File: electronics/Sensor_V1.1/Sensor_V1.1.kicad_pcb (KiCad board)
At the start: 2 copper layers, 45.9 x 25.6 mm, 34 parts, among them J1 nuclone_small_left, J2 nuclone_small_right, J5 DevBoardUartInput, Q1 DMG1012, Q2 DMG1012, Q3 DMG1012, U1 PPG_sensor, U2 reference_sot23-3, U3 MCP6541

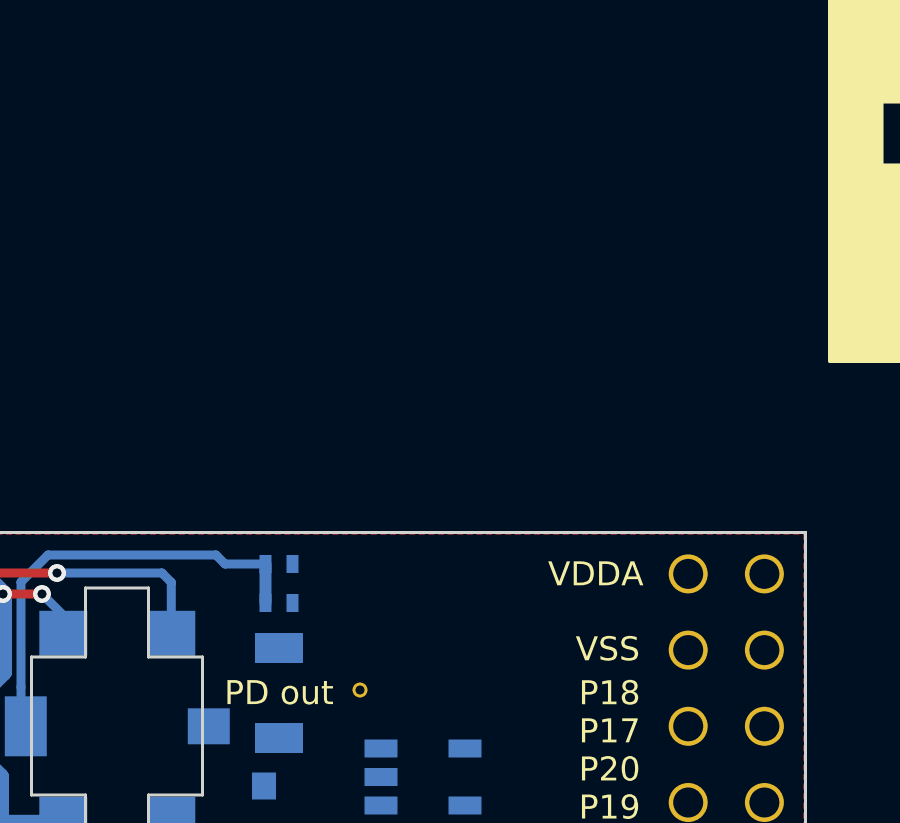
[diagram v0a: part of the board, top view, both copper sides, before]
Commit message: starting to move analog stuff to VSSA and then to star grounds/vcc's. imported net ties
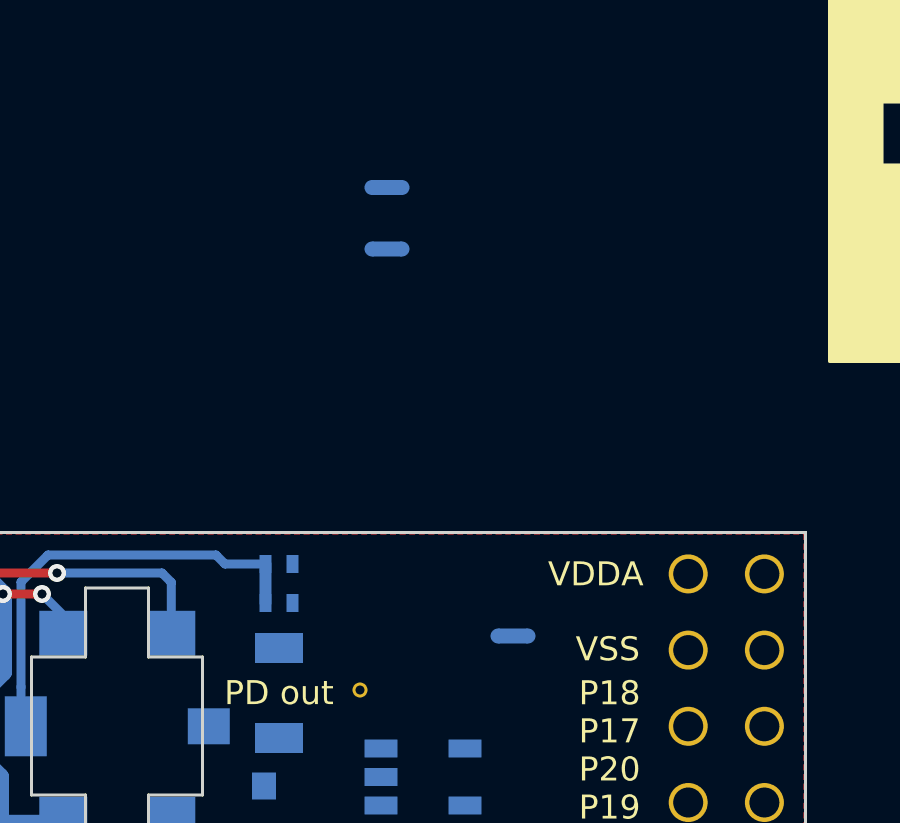
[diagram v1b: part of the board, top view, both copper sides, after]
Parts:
- added NT1: VSS_PD, NetTie:NetTie-2_SMD_Pad0.5mm, B.Cu at (94.1, 64.1)
- added NT2: VSS_CMP, NetTie:NetTie-2_SMD_Pad0.5mm, B.Cu at (94.1, 62.0)
- added NT3: VDD_CMP, NetTie:NetTie-2_SMD_Pad0.5mm, B.Cu at (98.3, 77.0)
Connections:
- C10 pad 2: /VSSA -> /VSS_CMP
- U3 pad 2: /VSSA -> /VSS_CMP
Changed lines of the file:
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@@
     (tracks 79)
     (zones 0)
-    (modules 34)
-    (nets 50)
+    (modules 37)
+    (nets 52)
   )
   (page A4)
@@
   (net 48 /PIO0_20)
   (net 49 /PIO0_19)
+  (net 50 /VSS_CMP)
+  (net 51 /VDD_CMP)
   (net_class Default "This is the default net class."
     (clearance 0.127)
@@
     (add_net /VDD)
     (add_net /VDDA)
+    (add_net /VDD_CMP)
     (add_net /VREF)
     (add_net /VSS)
     (add_net /VSSA)
+    (add_net /VSS_CMP)
     (add_net /VSS_PD)
     (add_net "Net-(J1-Pad11)")
@@
     (add_net "Net-(R17-Pad2)")
   )
+  (module NetTie:NetTie-2_SMD_Pad0.5mm (layer B.Cu)
+    (at 98.3 77)
+    (descr "Net tie, 2 pin, 0.5mm square SMD pads")
+    (tags "net tie")
+    (attr virtual)
+    (fp_text reference NT3 (at 0 1.2) (layer B.SilkS)
+      (effects (font (size 1 1) (thickness 0.15)) (justify mirror))
+    )
+    (fp_text value VDD_CMP (at 0 -1.2) (layer B.Fab)
+      (effects (font (size 1 1) (thickness 0.15)) (justify mirror))
+    )
+    (fp_poly (pts (xy -0.5 0.25) (xy 0.5 0.25) (xy 0.5 -0.25) (xy -0.5 -0.25)) (layer B.Cu) (width 0))
+    (fp_line (start 1 0.5) (end -1 0.5) (layer B.CrtYd) (width 0.05))
+    (fp_line (start 1 -0.5) (end 1 0.5) (layer B.CrtYd) (width 0.05))
+    (fp_line (start -1 -0.5) (end 1 -0.5) (layer B.CrtYd) (width 0.05))
+    (fp_line (start -1 0.5) (end -1 -0.5) (layer B.CrtYd) (width 0.05))
+    (pad 2 smd circle (at 0.5 0) (size 0.5 0.5) (layers B.Cu)
+      (net 51 /VDD_CMP))
+    (pad 1 smd circle (at -0.5 0) (size 0.5 0.5) (layers B.Cu)
+      (net 3 /VDD))
+  )
+  (module NetTie:NetTie-2_SMD_Pad0.5mm (layer B.Cu)
+    (at 94.1 62.05)
+    (descr "Net tie, 2 pin, 0.5mm square SMD pads")
+    (tags "net tie")
+    (attr virtual)
+    (fp_text reference NT2 (at 0 1.2) (layer B.SilkS)
+      (effects (font (size 1 1) (thickness 0.15)) (justify mirror))
+    )
+    (fp_text value VSS_CMP (at 0 -1.2) (layer B.Fab)
+      (effects (font (size 1 1) (thickness 0.15)) (justify mirror))
+    )
+    (fp_poly (pts (xy -0.5 0.25) (xy 0.5 0.25) (xy 0.5 -0.25) (xy -0.5 -0.25)) (layer B.Cu) (width 0))
+    (fp_line (start 1 0.5) (end -1 0.5) (layer B.CrtYd) (width 0.05))
+    (fp_line (start 1 -0.5) (end 1 0.5) (layer B.CrtYd) (width 0.05))
+    (fp_line (start -1 -0.5) (end 1 -0.5) (layer B.CrtYd) (width 0.05))
+    (fp_line (start -1 0.5) (end -1 -0.5) (layer B.CrtYd) (width 0.05))
+    (pad 2 smd circle (at 0.5 0) (size 0.5 0.5) (layers B.Cu)
+      (net 50 /VSS_CMP))
+    (pad 1 smd circle (at -0.5 0) (size 0.5 0.5) (layers B.Cu)
+      (net 2 /VSS))
+  )
+  (module NetTie:NetTie-2_SMD_Pad0.5mm (layer B.Cu)
+    (at 94.1 64.1)
+    (descr "Net tie, 2 pin, 0.5mm square SMD pads")
+    (tags "net tie")
+    (attr virtual)
+    (fp_text reference NT1 (at 0 1.2) (layer B.SilkS)
+      (effects (font (size 1 1) (thickness 0.15)) (justify mirror))
+    )
+    (fp_text value VSS_PD (at 0 -1.2) (layer B.Fab)
+      (effects (font (size 1 1) (thickness 0.15)) (justify mirror))
+    )
+    (fp_poly (pts (xy -0.5 0.25) (xy 0.5 0.25) (xy 0.5 -0.25) (xy -0.5 -0.25)) (layer B.Cu) (width 0))
+    (fp_line (start 1 0.5) (end -1 0.5) (layer B.CrtYd) (width 0.05))
+    (fp_line (start 1 -0.5) (end 1 0.5) (layer B.CrtYd) (width 0.05))
+    (fp_line (start -1 -0.5) (end 1 -0.5) (layer B.CrtYd) (width 0.05))
+    (fp_line (start -1 0.5) (end -1 -0.5) (layer B.CrtYd) (width 0.05))
+    (pad 2 smd circle (at 0.5 0) (size 0.5 0.5) (layers B.Cu)
+      (net 43 /VSS_PD))
+    (pad 1 smd circle (at -0.5 0) (size 0.5 0.5) (layers B.Cu)
+      (net 2 /VSS))
+  )
   (module SquantorRcl:R_0402_hand (layer B.Cu)
     (at 97 84.7 90)
@@
     (fp_line (start 0 0.2) (end 0 -0.2) (layer B.SilkS) (width 0.15))
     (pad 2 smd rect (at 0.55 0 180) (size 0.6 0.6) (layers B.Cu B.Paste B.Mask)
-      (net 5 /VSSA))
+      (net 50 /VSS_CMP))
     (pad 1 smd rect (at -0.55 0 180) (size 0.6 0.6) (layers B.Cu B.Paste B.Mask)
       (net 4 /VDDA))
@@
       (net 14 /PD_OUT))
     (pad 2 smd rect (at 0 -1.4 90) (size 0.6 1.1) (layers B.Cu B.Paste B.Mask)
-      (net 5 /VSSA))
+      (net 50 /VSS_CMP))
     (pad 1 smd rect (at -0.95 -1.4 90) (size 0.6 1.1) (layers B.Cu B.Paste B.Mask)
       (net 18 /CMP_OUT))

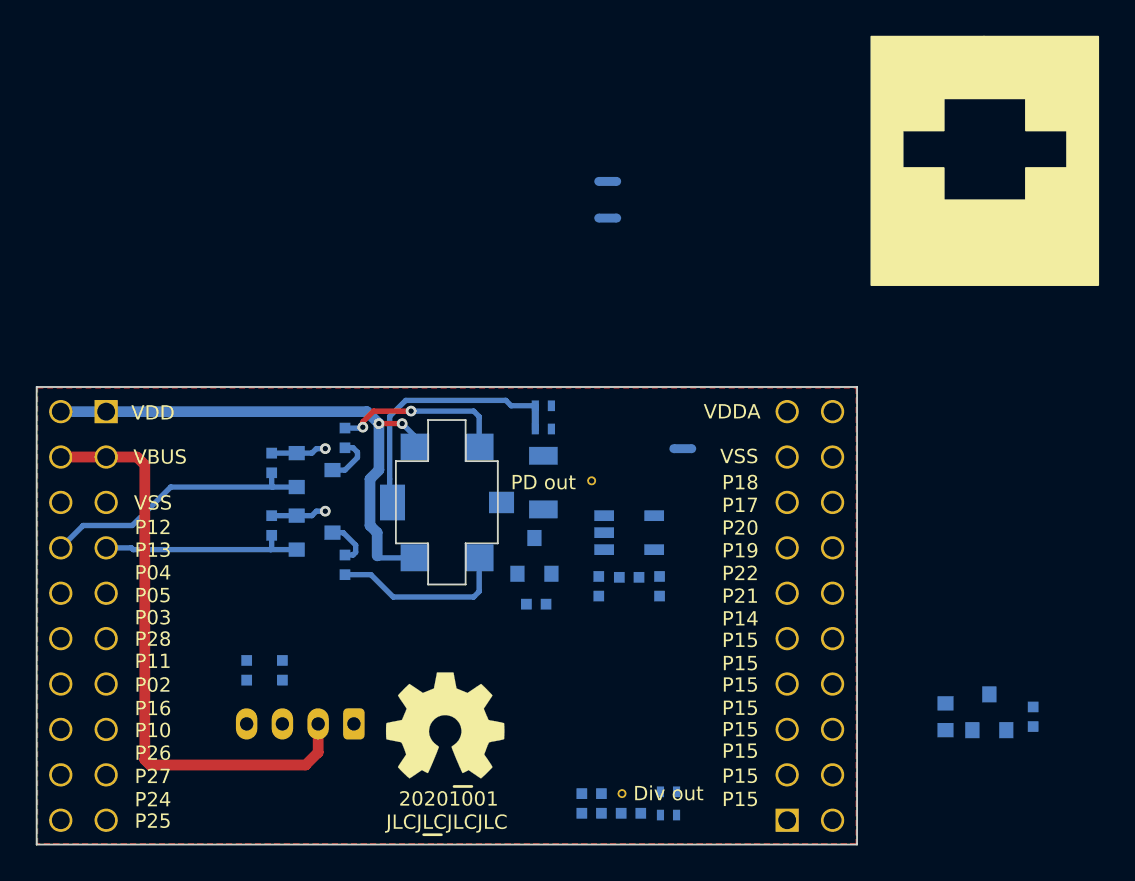
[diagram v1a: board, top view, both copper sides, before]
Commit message: placement of components
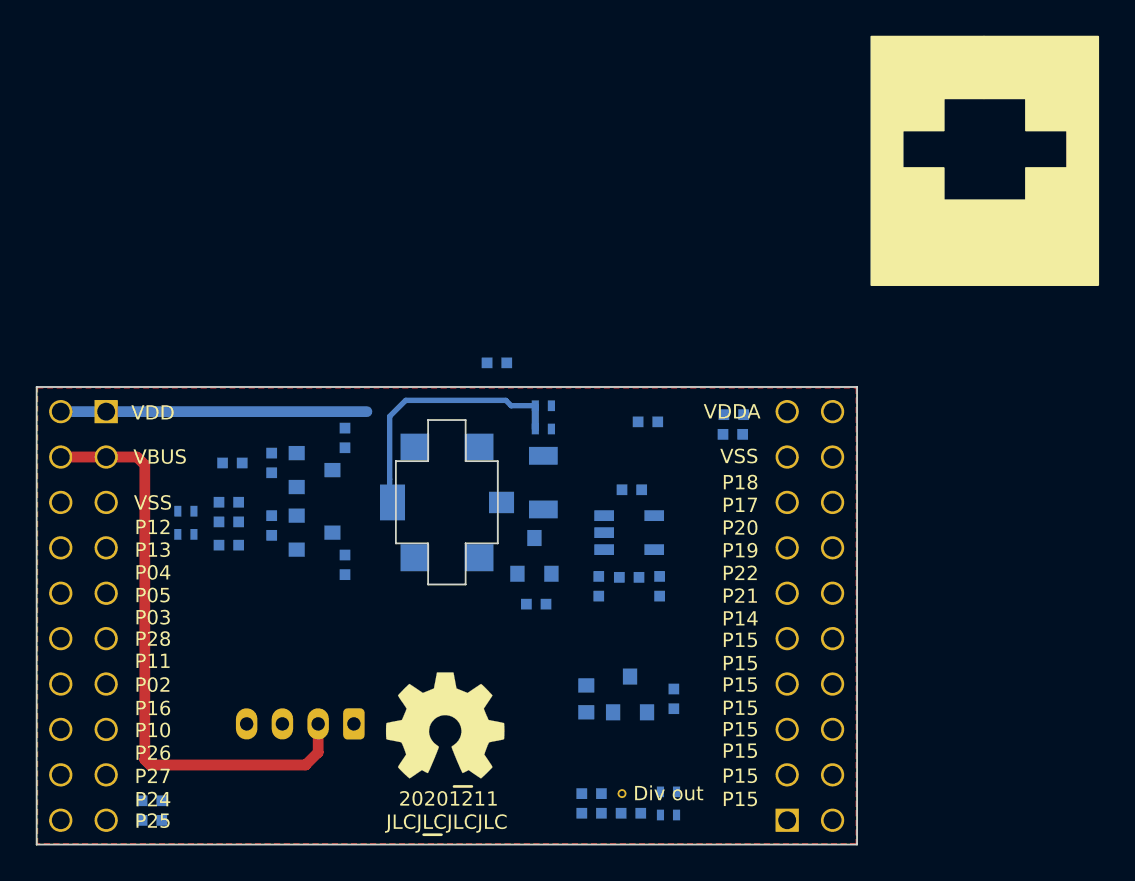
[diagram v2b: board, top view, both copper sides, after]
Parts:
- removed NT1: VSS_PD, NetTie:NetTie-2_SMD_Pad0.5mm
- removed NT2: VSS_CMP, NetTie:NetTie-2_SMD_Pad0.5mm
- removed NT3: VDD_CMP, NetTie:NetTie-2_SMD_Pad0.5mm
- removed TP10: PD out, SquantorTestPoints:TestPoint_hole_H03R05
- added C1: 1u, SquantorRcl:C_0402, B.Cu at (87.9, 72.2)
- added C2: 100n, SquantorRcl:C_0402, B.Cu at (72.9, 81.1)
- added C3: 100n, SquantorRcl:C_0402, B.Cu at (72.9, 82.4)
- added FB1: Ferrite_Bead, SquantorRcl:L_0402, B.Cu at (101.2, 75.1)
- added FB2: Ferrite_Bead, SquantorRcl:L_0402, B.Cu at (101.1, 76.2)
- added FB3: Ferrite_Bead, SquantorRcl:L_0402, B.Cu at (96.3, 75.5)
- added JP2: LED_VDD, SquantorSpecial:solder_jumper_2way_noconn, B.Cu at (70.5, 81.8)
- added JP6: LED_VBUS, SquantorSpecial:solder_jumper_2way_noconn, B.Cu at (70.5, 80.5)
- added R10: 1K, SquantorRcl:R_0402_hand, B.Cu at (73.1, 77.8)
- added R11: 1K, SquantorRcl:R_0402_hand, B.Cu at (72.9, 80.0)
- added R9: 0, SquantorRcl:R_0402_hand, B.Cu at (95.5, 79.3)
- N2: value 20201001 -> 20201211
- R3, R4: value 1K -> 100
- moved C5 20.1 mm to (97.8, 91.0)
- moved U2 20.1 mm to (95.3, 90.8)
- moved C6 20.1 mm to (92.9, 91.0)
- moved R2 11.1 mm to (68.6, 97.8), turned to 0 degrees
- moved R1 9.02 mm to (68.6, 96.7), turned to 0 degrees
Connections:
- net /LED1 renamed /LED1_C
- net /LED2 renamed /LED2_C
- net /PIO0_19 renamed Net-(J2-Pad13)
- net /PIO0_20 renamed Net-(J2-Pad14)
- net /PIO_11 renamed Net-(J1-Pad14)
- net /PIO_3 renamed Net-(J1-Pad12)
- C10 pad 1: /VDDA -> Net-(C10-Pad1)
- C10 pad 2: /VSS_CMP -> /VSS
- C11 pad 1: /VSSA -> /VSS
- C5 pad 1: /VDD -> Net-(C5-Pad1)
- C9 pad 2: /VSS_PD -> /VSS
- J1 pad 3: /VBUS -> Net-(J1-Pad3)
- J1 pad 5: /VSS -> Net-(J1-Pad5)
- J2 pad 15: /PIO0_17 -> /CMP_OUT
- J2 pad 16: /PIO0_18 -> /PD_ADC
- J2 pad 17: /VSS -> Net-(J2-Pad17)
- R12 pad 1: /VSSA -> /VSS
- U1 pad 1: /VDD -> /LED1_A
- U1 pad 3: /VDD -> /LED2_A
- U2 pad 1: /VDD -> Net-(C5-Pad1)
- U3 pad 2: /VSS_CMP -> /VSS
- U3 pad 5: /VDDA -> Net-(C10-Pad1)
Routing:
- net /LED2_EN: track 15.4 -> 0.00 mm
- net /VDD: track 30.9 -> 17.1 mm, vias 2 -> 0
- net /LED1_EN: track 11.5 -> 0.00 mm
- net /LED1_C: track 10.0 -> 0.00 mm
- net /LED2_C: track 9.91 -> 0.00 mm, vias 2 -> 0
- net /VSS: track 6.21 -> 0.00 mm, vias 2 -> 0
- net Net-(Q3-Pad3): track 2.79 -> 0.00 mm
- net Net-(Q2-Pad3): track 2.65 -> 0.00 mm

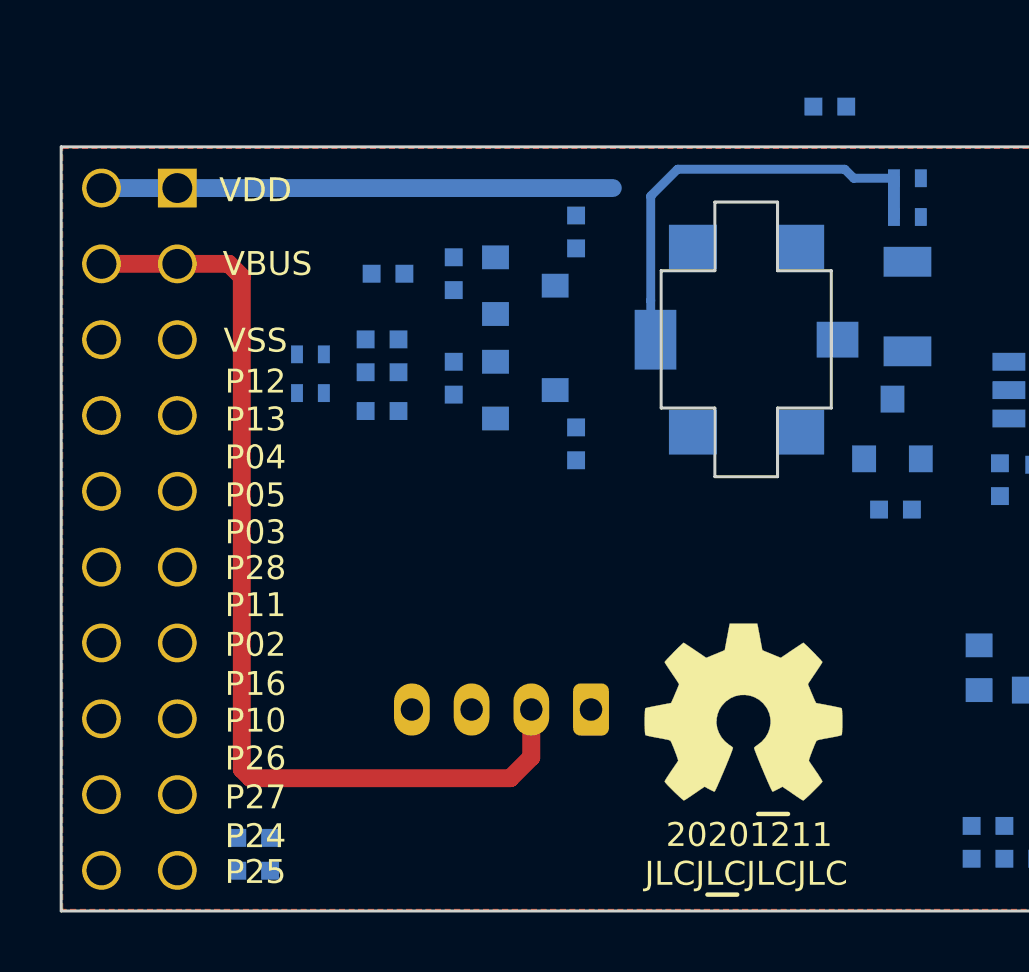
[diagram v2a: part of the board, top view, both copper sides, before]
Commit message: updated schematic into PCB
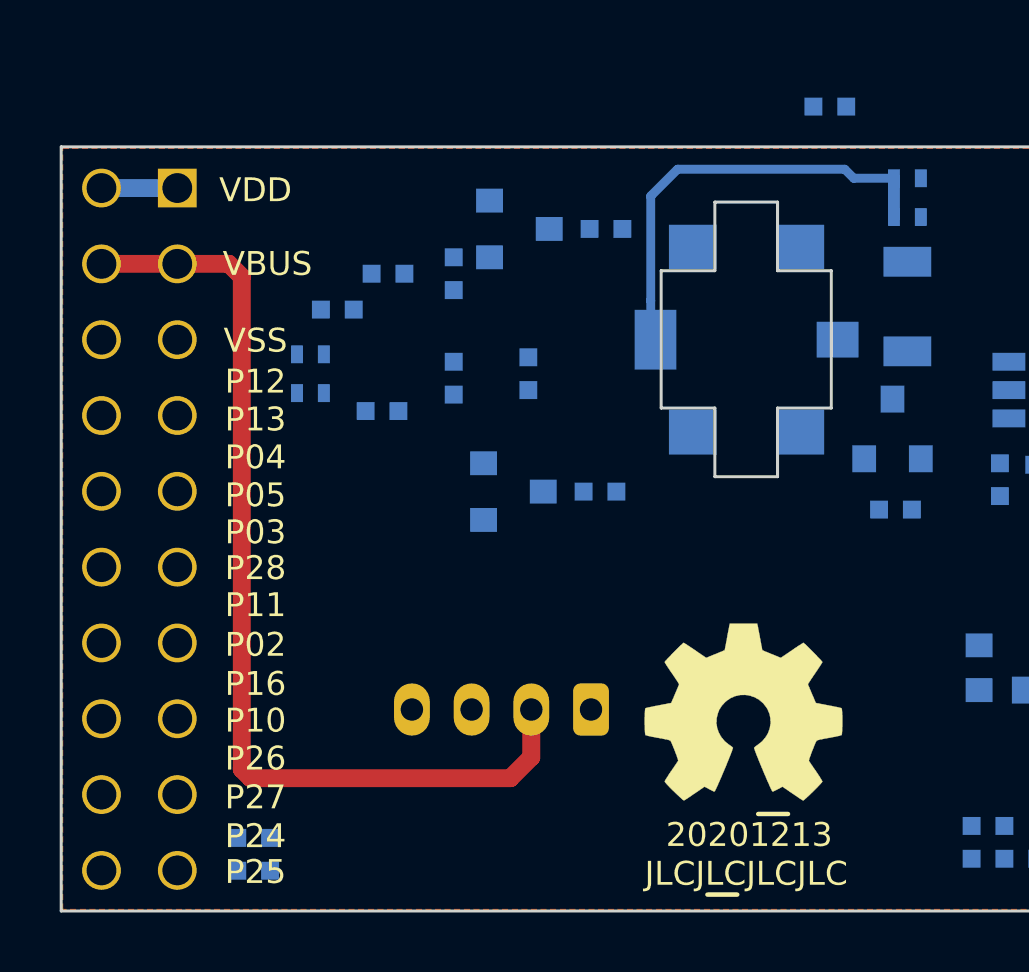
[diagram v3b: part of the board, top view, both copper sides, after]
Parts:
- N2: value 20201211 -> 20201213
- moved C2 4.90 mm to (77.8, 81.2), turned to 270 degrees
- moved Q2 3.42 mm to (77.3, 85.1)
- moved Q3 1.91 mm to (77.5, 76.3)
- moved R11 1.80 mm to (71.4, 79.0)
- moved R3 1.79 mm to (80.2, 85.1), turned to 180 degrees
- moved R4 1.00 mm to (80.4, 76.3), turned to 180 degrees
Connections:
- FB3 pad 1: /VSS -> Net-(FB3-Pad1)
- JP1 pad 2: /PD_BIAS -> Net-(FB3-Pad1)
- JP3 pad 2: /PD_BIAS -> Net-(FB3-Pad1)
- Q2 pad 2: /VSS -> Net-(Q2-Pad2)
- Q2 pad 3: Net-(Q2-Pad3) -> /LED1_C
- Q3 pad 2: /VSS -> Net-(Q3-Pad2)
- Q3 pad 3: Net-(Q3-Pad3) -> /LED2_C
- R3 pad 1: /LED1_C -> Net-(Q2-Pad2)
- R3 pad 2: Net-(Q2-Pad3) -> /VSS
- R4 pad 1: /LED2_C -> Net-(Q3-Pad2)
- R4 pad 2: Net-(Q3-Pad3) -> /VSS
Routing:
- net /VDD: track 17.1 -> 2.54 mm
